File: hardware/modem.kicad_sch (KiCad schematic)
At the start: 37 parts, among them J11 Conn_01x02, Q3 PMOS, Q4 Q_NPN_BEC, U6 SN74AVC4T245PW, U7 SARA-R500S-61B

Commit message: HW: Ready for routing
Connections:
- net +3.3V_MDM_UNFILTERED: now reaches C21.1, C24.1, C25.1, C26.1, C27.1, FB3.2, Q3.1 (D)
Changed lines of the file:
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@@
+		)
+	)
+	(label "+3.3V_MDM_UNFILTERED"
+		(at 35.56 87.63 0)
+		(fields_autoplaced yes)
+		(effects
+			(font
+				(size 1.27 1.27)
+			)
+			(justify left bottom)
 		)
 	)

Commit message: HW: Initial layout and routing done
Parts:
- L2: footprint Inductor_SMD:L_0603_1608Metric -> Inductor_SMD:L_0402_1005Metric
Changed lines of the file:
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@@
 	(title_block
 		(title "Iida devkit")
-		(date "2024-09-08")
+		(date "2024-09-10")
 		(rev "v4.0.0")
 	)
@@
 			)
 		)
-		(property "Footprint" "Inductor_SMD:L_0603_1608Metric"
+		(property "Footprint" "Inductor_SMD:L_0402_1005Metric"
 			(at 62.23 185.42 0)
 			(effects

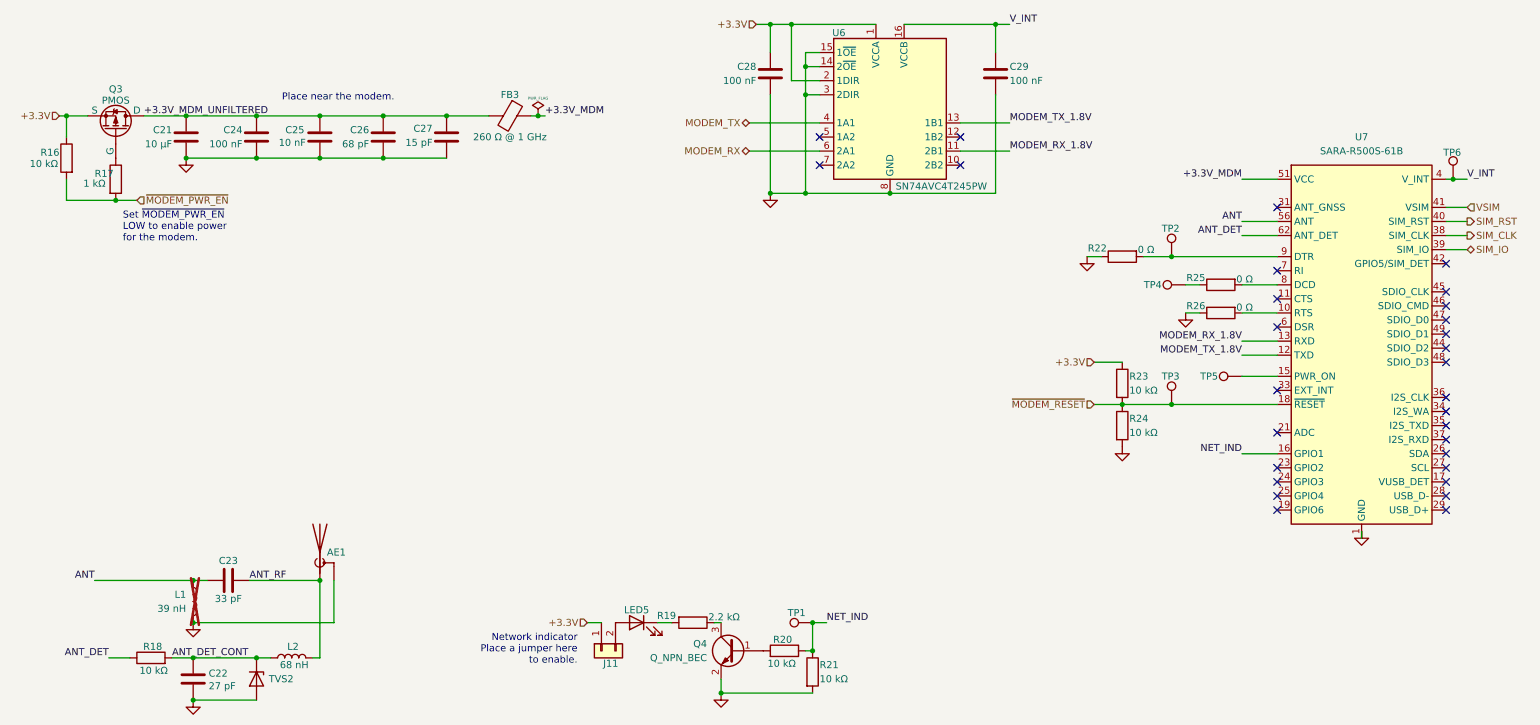
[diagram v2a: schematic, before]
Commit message: HW: Update schematic
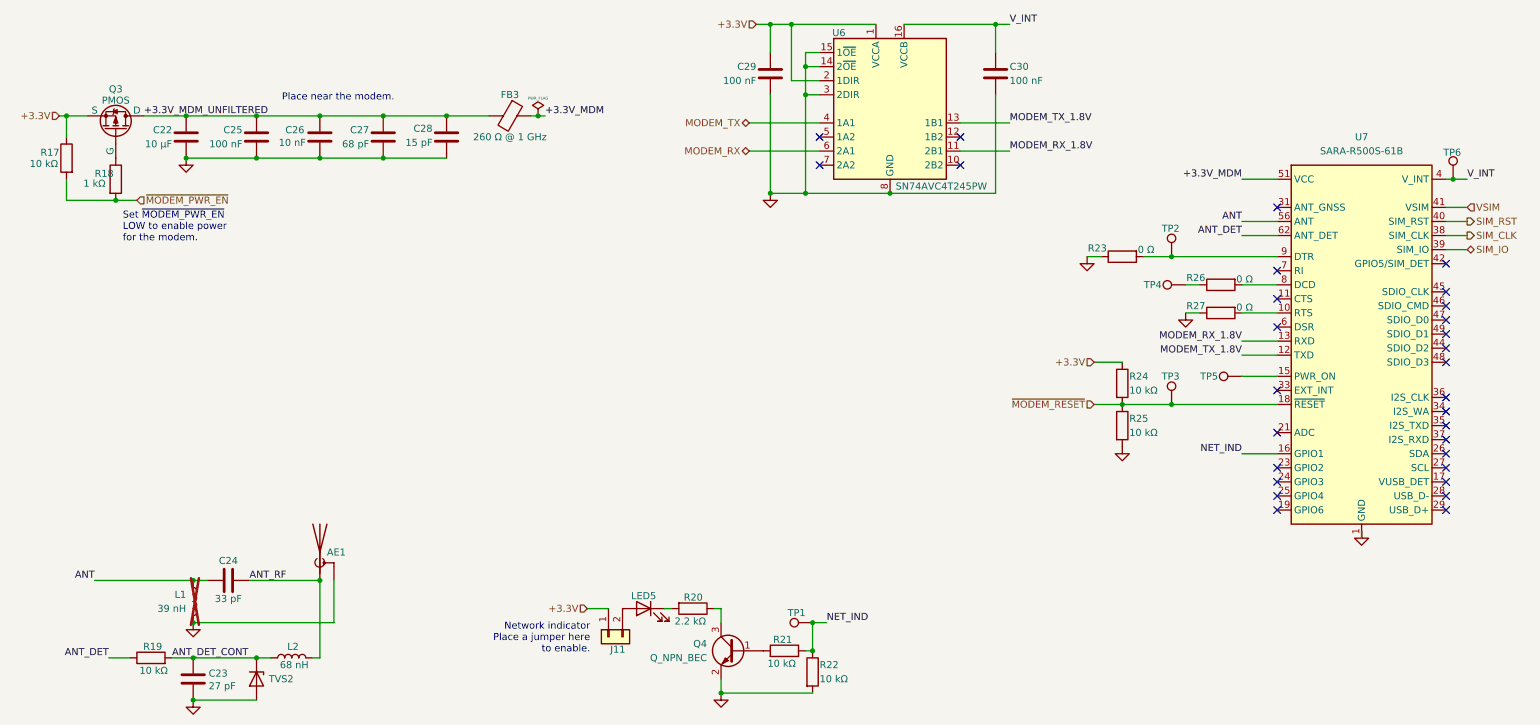
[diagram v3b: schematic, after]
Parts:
- TP1, TP2, TP3, TP4, TP5, TP6: footprint TestPoint:TestPoint_Pad_D2.5mm -> TestPoint:TestPoint_Pad_D1.5mm
- renumbered C21 to C22, C22 to C23, C23 to C24, C24 to C25, C25 to C26, C26 to C27, C27 to C28, C28 to C29, C29 to C30, R16 to R17, R17 to R18, R18 to R19, R19 to R20, R20 to R21, R21 to R22, R22 to R23, R23 to R24, R24 to R25, R25 to R26, R26 to R27
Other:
- moved on the sheet: J11, LED5, R20

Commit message: HW: Add PCB antenna option
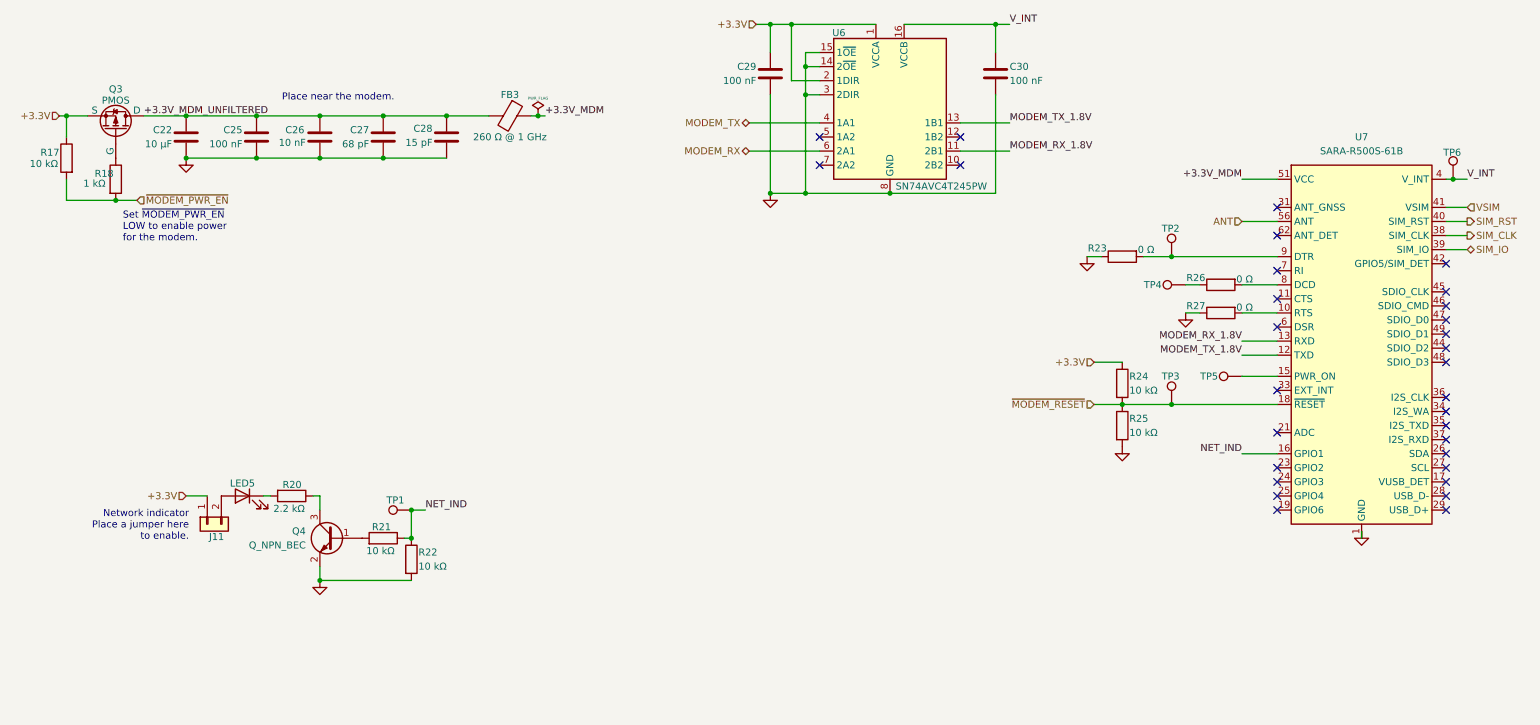
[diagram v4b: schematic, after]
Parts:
- removed AE1: Antenna, Connector_Coaxial:U.FL_Hirose_U.FL-R-SMT-1_Vertical, symbol Device:Antenna_Shield
- removed C23: 27 pF, perfect_footprints:0402_1005_perfect, symbol Device:C
- removed C24: 33 pF, perfect_footprints:0402_1005_perfect, symbol Device:C
- removed L1: 39 nH, Inductor_SMD:L_0603_1608Metric, symbol Device:L
- removed L2: 68 nH, Inductor_SMD:L_0402_1005Metric, symbol Device:L
- removed R19: 10 kΩ, perfect_footprints:0402_1005_perfect, symbol Device:R
- removed TVS2: PE1605M1Q_R1_00001, Diode_SMD:D_0402_1005Metric, symbol Device:D_Zener
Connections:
- net ANT_DET: no longer names the net of U7.62 (ANT_DET)
- no-connect marks 30 -> 31
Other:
- moved on the sheet: J11, LED5, Q4, R20, R21, R22, TP1

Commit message: HW: Cleanup schematic
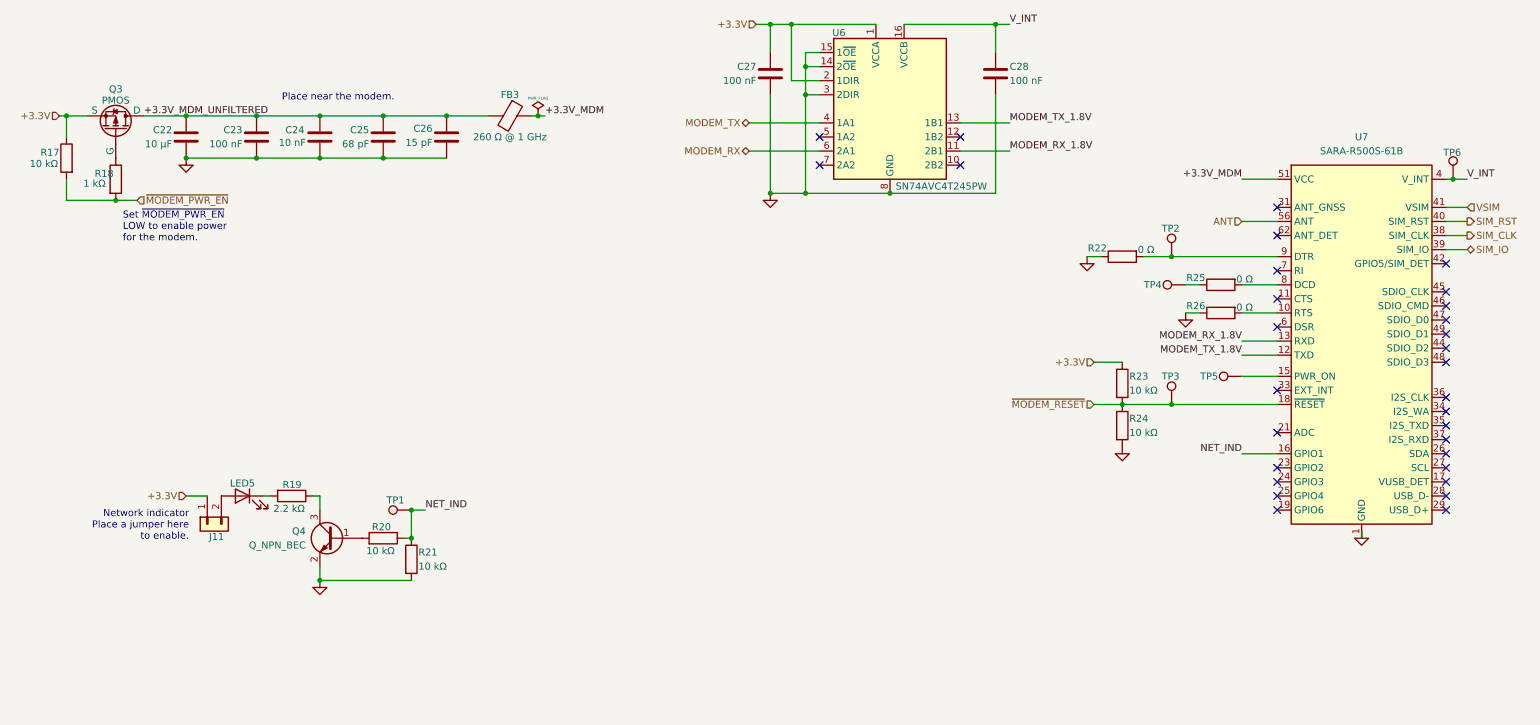
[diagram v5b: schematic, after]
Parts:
- renumbered C25 to C23, C26 to C24, C27 to C25, C28 to C26, C29 to C27, C30 to C28, R20 to R19, R21 to R20, R22 to R21, R23 to R22, R24 to R23, R25 to R24, R26 to R25, R27 to R26
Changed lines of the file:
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@@
 		(on_board yes)
 		(dnp no)
-		(property "Reference" "C26"
+		(property "Reference" "C24"
 			(at 64.516 90.17 0)
 			(effects
@@
 			(project "iida_devkit"
 				(path "/b12a6e25-97fb-4aba-bc96-af8db389bb9a/3723475b-e956-4027-ac40-e47346743900"
-					(reference "C26")
+					(reference "C24")
 					(unit 1)
 				)
@@
 		(on_board yes)
 		(dnp no)
-		(property "Reference" "R24"
+		(property "Reference" "R23"
 			(at 213.36 134.62 0)
 			(effects
@@
 			(project "iida_devkit"
 				(path "/b12a6e25-97fb-4aba-bc96-af8db389bb9a/3723475b-e956-4027-ac40-e47346743900"
-					(reference "R24")
+					(reference "R23")
 					(unit 1)
 				)
@@
 		(on_board yes)
 		(dnp no)
-		(property "Reference" "R21"
+		(property "Reference" "R20"
 			(at 76.708 161.798 90)
 			(effects
@@
 			(project "iida_devkit"
 				(path "/b12a6e25-97fb-4aba-bc96-af8db389bb9a/3723475b-e956-4027-ac40-e47346743900"
-					(reference "R21")
+					(reference "R20")
 					(unit 1)
 				)
@@
 		(on_board yes)
 		(dnp no)
-		(property "Reference" "R25"
+		(property "Reference" "R24"
 			(at 213.36 142.24 0)
 			(effects
@@
 			(project "iida_devkit"
 				(path "/b12a6e25-97fb-4aba-bc96-af8db389bb9a/3723475b-e956-4027-ac40-e47346743900"
-					(reference "R25")
+					(reference "R24")
 					(unit 1)
 				)
@@
 		(on_board yes)
 		(dnp no)
-		(property "Reference" "R22"
+		(property "Reference" "R21"
 			(at 85.09 166.37 0)
 			(effects
@@
 			(project "iida_devkit"
 				(path "/b12a6e25-97fb-4aba-bc96-af8db389bb9a/3723475b-e956-4027-ac40-e47346743900"
-					(reference "R22")
+					(reference "R21")
 					(unit 1)
 				)
@@
 		(on_board yes)
 		(dnp no)
-		(property "Reference" "C27"
+		(property "Reference" "C25"
 			(at 76.2 90.17 0)
 			(effects
@@
 			(project "iida_devkit"
 				(path "/b12a6e25-97fb-4aba-bc96-af8db389bb9a/3723475b-e956-4027-ac40-e47346743900"
-					(reference "C27")
+					(reference "C25")
 					(unit 1)
 				)
@@
 		(dnp no)
 		(fields_autoplaced yes)
-		(property "Reference" "#PWR023"
+		(property "Reference" "#PWR021"
 			(at 212.09 153.67 0)
 			(effects
@@
 			(project "iida_devkit"
 				(path "/b12a6e25-97fb-4aba-bc96-af8db389bb9a/3723475b-e956-4027-ac40-e47346743900"
-					(reference "#PWR023")
+					(reference "#PWR021")
 					(unit 1)
 				)
@@
 		(dnp no)
 		(fields_autoplaced yes)
-		(property "Reference" "#PWR022"
+		(property "Reference" "#PWR020"
 			(at 205.74 119.38 0)
 			(effects
@@
 			(project "iida_devkit"
 				(path "/b12a6e25-97fb-4aba-bc96-af8db389bb9a/3723475b-e956-4027-ac40-e47346743900"
-					(reference "#PWR022")
+					(reference "#PWR020")
 					(unit 1)
 				)
@@
 		(dnp no)
 		(fields_autoplaced yes)
-		(property "Reference" "#PWR025"
+		(property "Reference" "#PWR023"
 			(at 255.27 168.91 0)
 			(effects
@@
 			(project "iida_devkit"
 				(path "/b12a6e25-97fb-4aba-bc96-af8db389bb9a/3723475b-e956-4027-ac40-e47346743900"
-					(reference "#PWR025")
+					(reference "#PWR023")
 					(unit 1)
 				)
@@
 		(on_board yes)
 		(dnp no)
-		(property "Reference" "C30"
+		(property "Reference" "C28"
 			(at 191.77 78.74 0)
 			(effects
@@
 			(project "iida_devkit"
 				(path "/b12a6e25-97fb-4aba-bc96-af8db389bb9a/3723475b-e956-4027-ac40-e47346743900"
-					(reference "C30")
+					(reference "C28")
 					(unit 1)
 				)
@@
 		(on_board yes)
 		(dnp no)
-		(property "Reference" "C29"
+		(property "Reference" "C27"
 			(at 146.05 78.74 0)
 			(effects
@@
 			(project "iida_devkit"
 				(path "/b12a6e25-97fb-4aba-bc96-af8db389bb9a/3723475b-e956-4027-ac40-e47346743900"
-					(reference "C29")
+					(reference "C27")
 					(unit 1)
 				)
@@
 		(on_board yes)
 		(dnp no)
-		(property "Reference" "R27"
+		(property "Reference" "R26"
 			(at 227.076 121.92 90)
 			(effects
@@
 			(project "iida_devkit"
 				(path "/b12a6e25-97fb-4aba-bc96-af8db389bb9a/3723475b-e956-4027-ac40-e47346743900"
-					(reference "R27")
+					(reference "R26")
 					(unit 1)
 				)
@@
 		(on_board yes)
 		(dnp no)
-		(property "Reference" "R20"
+		(property "Reference" "R19"
 			(at 64.008 154.178 90)
 			(effects
@@
 			(project "iida_devkit"
 				(path "/b12a6e25-97fb-4aba-bc96-af8db389bb9a/3723475b-e956-4027-ac40-e47346743900"
-					(reference "R20")
+					(reference "R19")
 					(unit 1)
 				)
@@
 		(on_board yes)
 		(dnp no)
-		(property "Reference" "C28"
+		(property "Reference" "C26"
 			(at 87.63 89.916 0)
 			(effects
@@
 			(project "iida_devkit"
 				(path "/b12a6e25-97fb-4aba-bc96-af8db389bb9a/3723475b-e956-4027-ac40-e47346743900"
-					(reference "C28")
+					(reference "C26")
 					(unit 1)
 				)
@@
 		(on_board yes)
 		(dnp no)
-		(property "Reference" "C25"
+		(property "Reference" "C23"
 			(at 53.34 90.17 0)
 			(effects
@@
 			(project "iida_devkit"
 				(path "/b12a6e25-97fb-4aba-bc96-af8db389bb9a/3723475b-e956-4027-ac40-e47346743900"
-					(reference "C25")
+					(reference "C23")
 					(unit 1)
 				)
@@
 		(dnp no)
 		(fields_autoplaced yes)
-		(property "Reference" "#PWR021"
+		(property "Reference" "#PWR019"
 			(at 148.59 107.95 0)
 			(effects
@@
 			(project "iida_devkit"
 				(path "/b12a6e25-97fb-4aba-bc96-af8db389bb9a/3723475b-e956-4027-ac40-e47346743900"
-					(reference "#PWR021")
+					(reference "#PWR019")
 					(unit 1)
 				)
@@
 		(on_board yes)
 		(dnp no)
-		(property "Reference" "R23"
+		(property "Reference" "R22"
 			(at 209.296 111.506 90)
 			(effects
@@
 			(project "iida_devkit"
 				(path "/b12a6e25-97fb-4aba-bc96-af8db389bb9a/3723475b-e956-4027-ac40-e47346743900"
-					(reference "R23")
+					(reference "R22")
 					(unit 1)
 				)
@@
 		(dnp no)
 		(fields_autoplaced yes)
-		(property "Reference" "#PWR024"
+		(property "Reference" "#PWR022"
 			(at 223.52 129.54 0)
 			(effects
@@
 			(project "iida_devkit"
 				(path "/b12a6e25-97fb-4aba-bc96-af8db389bb9a/3723475b-e956-4027-ac40-e47346743900"
-					(reference "#PWR024")
+					(reference "#PWR022")
 					(unit 1)
 				)
@@
 		(on_board yes)
 		(dnp no)
-		(property "Reference" "R26"
+		(property "Reference" "R25"
 			(at 227.076 116.84 90)
 			(effects
@@
 			(project "iida_devkit"
 				(path "/b12a6e25-97fb-4aba-bc96-af8db389bb9a/3723475b-e956-4027-ac40-e47346743900"
-					(reference "R26")
+					(reference "R25")
 					(unit 1)
 				)
@@
 		(dnp no)
 		(fields_autoplaced yes)
-		(property "Reference" "#PWR020"
+		(property "Reference" "#PWR018"
 			(at 67.31 177.8 0)
 			(effects
@@
 			(project "iida_devkit"
 				(path "/b12a6e25-97fb-4aba-bc96-af8db389bb9a/3723475b-e956-4027-ac40-e47346743900"
-					(reference "#PWR020")
+					(reference "#PWR018")
 					(unit 1)
 				)
